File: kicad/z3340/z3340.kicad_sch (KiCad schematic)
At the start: 43 parts, among them J1 Conn_01x01, J2 Conn_01x02, J3 Conn_02x20_Odd_Even, Q3 MMBT3904, U1 DG442CY+, U10 AS3364, U11 PCA9555D, U13 TL074, U14 DG406, U15 M24C02-WMN, U5 TL074, U8 DG442CY+, U9 TL072

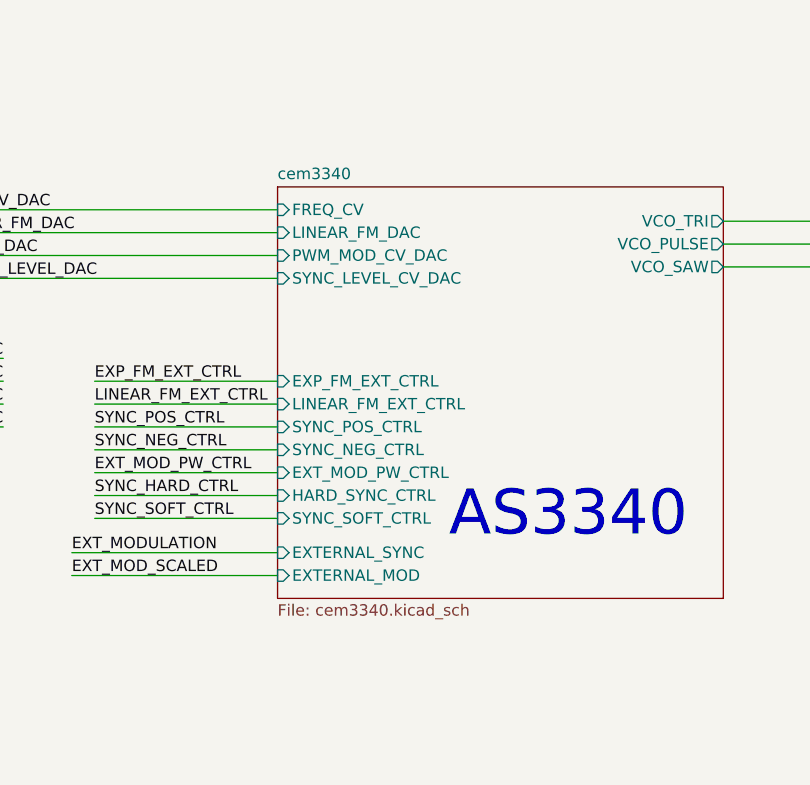
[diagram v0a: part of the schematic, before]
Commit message: continue file renaming
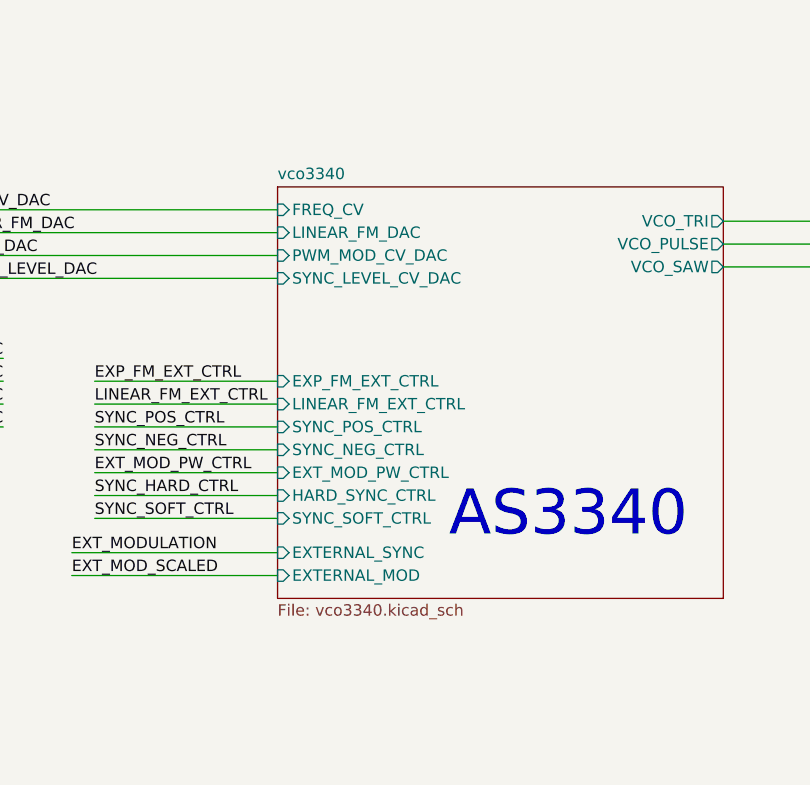
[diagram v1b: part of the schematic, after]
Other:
- sheet cem3340 renamed vco3340
- sheet vco3340: file cem3340.kicad_sch -> vco3340.kicad_sch

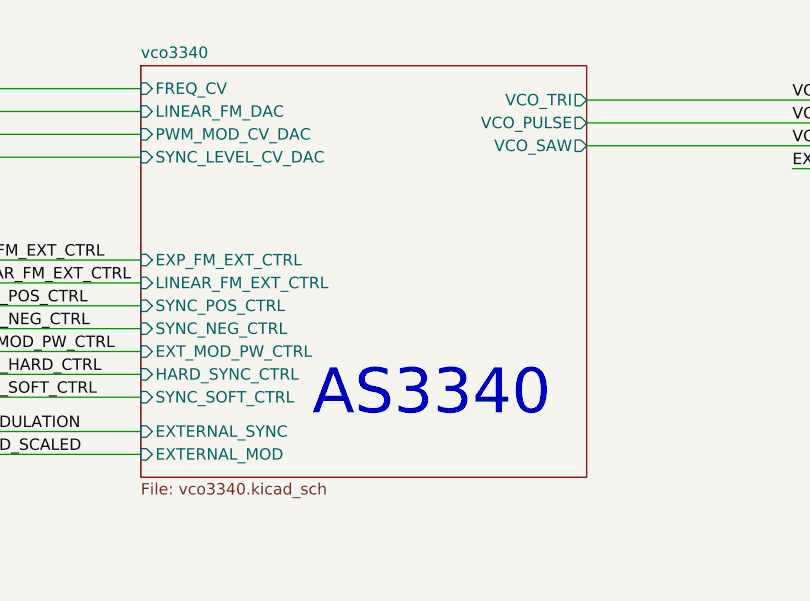
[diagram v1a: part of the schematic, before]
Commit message: cleanup references after file renaming
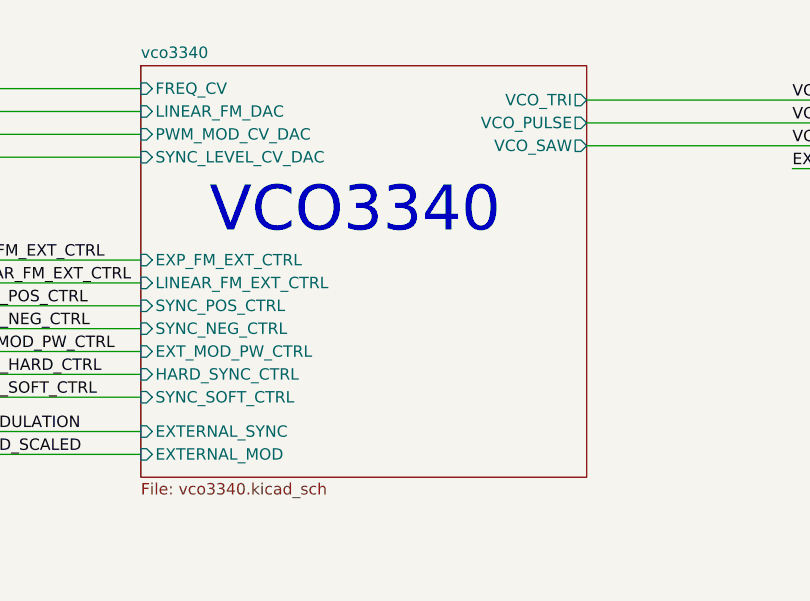
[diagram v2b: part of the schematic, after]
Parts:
- U10: symbol as3340:AS3364 -> z3340:AS3364
- U14: symbol as3340:DG406 -> z3340:DG406
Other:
- note added: "VCO3340"
- note removed: "AS3340"
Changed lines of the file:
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@@
     (effects (font (size 1.27 1.27)) (justify left bottom))
   )
-  (text "AS3340" (at 157.48 165.1 0)
+  (text "VCO3340" (at 146.05 144.78 0)
     (effects (font (size 5.0038 5.0038)) (justify left bottom))
   )
@@
     )
   )
-  (symbol (lib_id "as3340:DG406") (at 281.94 66.04 0) (unit 1)
+  (symbol (lib_id "z3340:DG406") (at 281.94 66.04 0) (unit 1)
     (in_bom yes) (on_board yes) (dnp no)
     (property "Reference" "U14" (at 279.4 64.77 0)
@@
     )
   )
-  (symbol (lib_id "as3340:AS3364") (at 125.73 236.22 0) (unit 1)
+  (symbol (lib_id "z3340:AS3364") (at 125.73 236.22 0) (unit 1)
     (in_bom yes) (on_board yes) (dnp no) (fields_autoplaced)
     (property "Reference" "U10" (at 132.7912 236.2779 0)

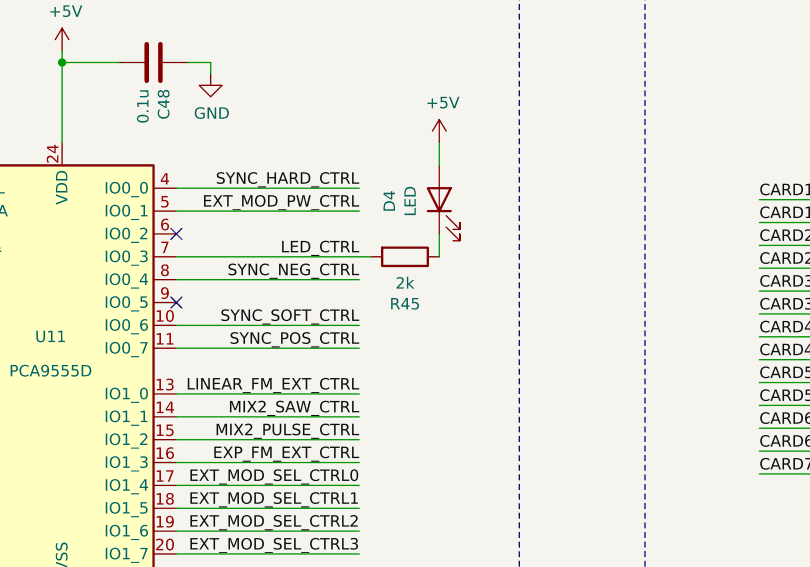
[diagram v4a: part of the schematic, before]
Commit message: updates for v0.9: polygons, LED resistor, mod amount
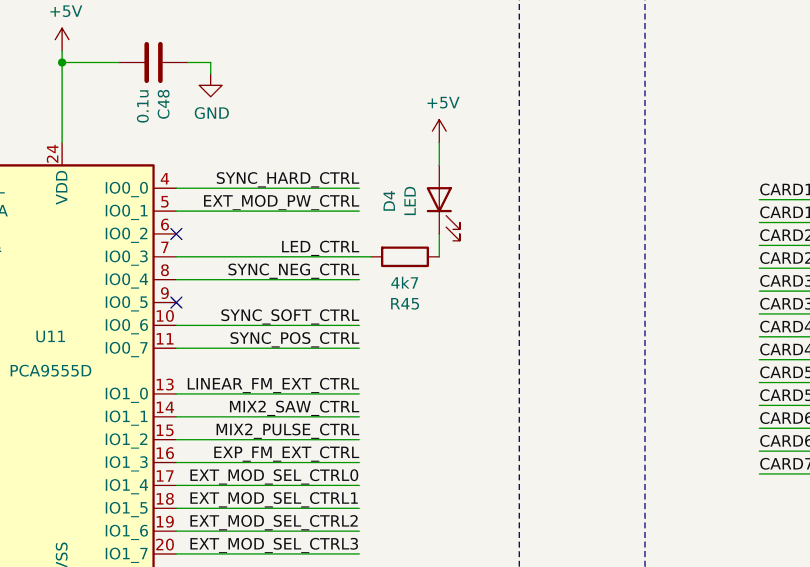
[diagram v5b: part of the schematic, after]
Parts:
- C12, C13, C19, C21, C22, C27, C37, C38, C40, C43, C44, C45, C46, C47, C48, C9: LCSC (none) -> C14663; LCSC Part C14663 -> (none)
- C30: LCSC (none) -> C53987; LCSC Part C53987 -> (none)
- D4: LCSC (none) -> C2286; LCSC Part C2286 -> (none)
- Q3: LCSC (none) -> C20526; LCSC Part C20526 -> (none)
- R40: LCSC (none) -> C22775; LCSC Part C22775 -> (none)
- R45: value 2k -> 4k7; LCSC (none) -> C23162; LCSC Part C22975 -> (none)
- R48, R65: LCSC (none) -> C25804; LCSC Part C25804 -> (none)
- R51, R57, R58: LCSC (none) -> C25803; LCSC Part C25803 -> (none)
- U1, U8: LCSC (none) -> C2673321; LCSC Part C2673321 -> (none)
- U11: LCSC (none) -> C83265; LCSC Part C83265 -> (none)
- U13, U5: LCSC (none) -> C96507; LCSC Part C96507 -> (none)
- U14: LCSC (none) -> C426318; LCSC Part C426318 -> (none)
- U15: LCSC (none) -> C7562; LCSC Part C7562 -> (none)
- U9: LCSC (none) -> C6961; LCSC Part C6961 -> (none)
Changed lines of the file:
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@@
   (title_block
     (title "Zoxnoxious 3340 Oscillator")
-    (date "2024-07-15")
-    (rev "0.8")
+    (date "2025-02-06")
+    (rev "0.9")
     (company "Zoxnoxious Engineering")
   )
@@
       (effects (font (size 1.27 1.27)) hide)
     )
-    (property "LCSC Part" "C14663" (at 189.23 29.21 0)
+    (property "LCSC" "C14663" (at 189.23 29.21 0)
       (effects (font (size 1.27 1.27)) hide)
     )
@@
       (effects (font (size 1.27 1.27)) hide)
     )
-    (property "LCSC Part" "C83265" (at 179.07 63.5 0)
+    (property "LCSC" "C83265" (at 179.07 63.5 0)
       (effects (font (size 1.27 1.27)) hide)
     )
@@
       (effects (font (size 1.27 1.27)))
     )
-    (property "Value" "2k" (at 217.17 53.7464 90)
+    (property "Value" "4k7" (at 217.17 53.7464 90)
       (effects (font (size 1.27 1.27)))
     )
@@
       (effects (font (size 1.27 1.27)) hide)
     )
-    (property "LCSC Part" "C22975" (at 217.17 50.8 0)
+    (property "LCSC" "C23162" (at 217.17 50.8 0)
       (effects (font (size 1.27 1.27)) hide)
     )
@@
       (effects (font (size 1.27 1.27)) hide)
     )
-    (property "LCSC Part" "C2286" (at 220.98 44.45 0)
+    (property "LCSC" "C2286" (at 220.98 44.45 0)
       (effects (font (size 1.27 1.27)) hide)
     )
@@
       (effects (font (size 1.27 1.27)) hide)
     )
-    (property "LCSC Part" "C14663" (at 386.08 29.21 0)
+    (property "LCSC" "C14663" (at 386.08 29.21 0)
       (effects (font (size 1.27 1.27)) hide)
     )
@@
       (effects (font (size 1.27 1.27)) hide)
     )
-    (property "LCSC Part" "C7562" (at 379.73 43.18 0)
+    (property "LCSC" "C7562" (at 379.73 43.18 0)
       (effects (font (size 1.27 1.27)) hide)
     )
@@
       (effects (font (size 1.27 1.27)) hide)
     )
-    (property "LCSC Part" "C14663" (at 153.67 231.14 0)
+    (property "LCSC" "C14663" (at 153.67 231.14 0)
       (effects (font (size 1.27 1.27)) hide)
     )
@@
       (effects (font (size 1.27 1.27)) hide)
     )
-    (property "LCSC Part" "C14663" (at 153.67 242.57 0)
+    (property "LCSC" "C14663" (at 153.67 242.57 0)
       (effects (font (size 1.27 1.27)) hide)
     )
@@
       (effects (font (size 1.27 1.27)) hide)
     )
-    (property "LCSC Part" "C2673321" (at 165.1 237.49 0)
+    (property "LCSC" "C2673321" (at 165.1 237.49 0)
       (effects (font (size 1.27 1.27)) hide)
     )
@@
       (effects (font (size 1.27 1.27)) hide)
     )
-    (property "LCSC Part" "C14663" (at 179.07 231.14 0)
+    (property "LCSC" "C14663" (at 179.07 231.14 0)
       (effects (font (size 1.27 1.27)) hide)
     )
@@
       (effects (font (size 1.27 1.27)) hide)
     )
-    (property "LCSC Part" "C14663" (at 179.07 242.57 0)
+    (property "LCSC" "C14663" (at 179.07 242.57 0)
       (effects (font (size 1.27 1.27)) hide)
     )
@@
       (effects (font (size 1.27 1.27)) hide)
     )
-    (property "LCSC Part" "C2673321" (at 190.5 237.49 0)
+    (property "LCSC" "C2673321" (at 190.5 237.49 0)
       (effects (font (size 1.27 1.27)) hide)
     )
@@
       (effects (font (size 1.27 1.27)) hide)
     )
-    (property "LCSC Part" "C14663" (at 125.73 254 0)
+    (property "LCSC" "C14663" (at 125.73 254 0)
       (effects (font (size 1.27 1.27)) hide)
     )
@@
       (effects (font (size 1.27 1.27)) hide)
     )
-    (property "LCSC Part" "C426318" (at 281.94 66.04 0)
+    (property "LCSC" "C426318" (at 281.94 66.04 0)
       (effects (font (size 1.27 1.27)) hide)
     )
@@
       (effects (font (size 1.27 1.27)) hide)
     )
-    (property "LCSC Part" "C25804" (at 332.74 207.01 0)
+    (property "LCSC" "C25804" (at 332.74 207.01 0)
       (effects (font (size 1.27 1.27)) hide)
     )
@@
       (effects (font (size 1.27 1.27)) hide)
     )
-    (property "LCSC Part" "C96507" (at 397.51 217.17 0)
+    (property "LCSC" "C96507" (at 397.51 217.17 0)
       (effects (font (size 1.27 1.27)) hide)
     )
@@
       (effects (font (size 1.27 1.27)) hide)
     )
-    (property "LCSC Part" "C14663" (at 270.51 29.21 0)
+    (property "LCSC" "C14663" (at 270.51 29.21 0)
       (effects (font (size 1.27 1.27)) hide)
     )
@@
       (effects (font (size 1.27 1.27)) hide)
     )
-    (property "LCSC Part" "C22775" (at 115.57 240.03 0)
+    (property "LCSC" "C22775" (at 115.57 240.03 0)
       (effects (font (size 1.27 1.27)) hide)
     )
@@
       (effects (font (size 1.27 1.27)) hide)
     )
-    (property "LCSC Part" "C6961" (at 317.5 53.34 0)
+    (property "LCSC" "C6961" (at 317.5 53.34 0)
       (effects (font (size 1.27 1.27)) hide)
     )
@@
       (effects (font (size 1.27 1.27)) hide)
     )
-    (property "LCSC Part" "C14663" (at 58.42 246.38 0)
+    (property "LCSC" "C14663" (at 58.42 246.38 0)
       (effects (font (size 1.27 1.27)) hide)
     )
@@
       (effects (font (size 1.27 1.27)) hide)
     )
-    (property "LCSC Part" "C6961" (at 99.06 238.76 0)
+    (property "LCSC" "C6961" (at 99.06 238.76 0)
       (effects (font (size 1.27 1.27)) hide)
     )
@@
       (effects (font (size 1.27 1.27)) (justify left) hide)
     )
-    (property "LCSC Part" "C20526" (at 330.2 218.44 0)
+    (property "LCSC" "C20526" (at 330.2 218.44 0)
       (effects (font (size 1.27 1.27)) hide)
     )
@@
       (effects (font (size 1.27 1.27)) hide)
     )
-    (property "LCSC Part" "C96507" (at 40.64 238.76 0)
+    (property "LCSC" "C96507" (at 40.64 238.76 0)
       (effects (font (size 1.27 1.27)) hide)
     )
@@
       (effects (font (size 1.27 1.27)) hide)
     )
-    (property "LCSC Part" "C14663" (at 86.36 234.95 0)
+    (property "LCSC" "C14663" (at 86.36 234.95 0)
       (effects (font (size 1.27 1.27)) hide)
     )
@@
       (effects (font (size 1.27 1.27)) hide)
     )
-    (property "LCSC Part" "C25803" (at 299.72 50.8 0)
+    (property "LCSC" "C25803" (at 299.72 50.8 0)
       (effects (font (size 1.27 1.27)) hide)
     )
@@
       (effects (font (size 1.27 1.27)) hide)
     )
-    (property "LCSC Part" "C14663" (at 86.36 246.38 0)
+    (property "LCSC" "C14663" (at 86.36 246.38 0)
       (effects (font (size 1.27 1.27)) hide)
     )
@@
       (effects (font (size 1.27 1.27)) hide)
     )
-    (property "LCSC Part" "C25803" (at 316.23 218.44 0)
+    (property "LCSC" "C25803" (at 316.23 218.44 0)
       (effects (font (size 1.27 1.27)) hide)
     )
@@
       (effects (font (size 1.27 1.27)) hide)
     )
-    (property "LCSC Part" "C25803" (at 314.96 43.18 0)
+    (property "LCSC" "C25803" (at 314.96 43.18 0)
       (effects (font (size 1.27 1.27)) hide)
     )
@@
       (effects (font (size 1.27 1.27)) hide)
     )
-    (property "LCSC" "" (at 27.94 246.38 0)
+    (property "LCSC" "C14663" (at 27.94 246.38 0)
       (effects (font (size 1.27 1.27)) hide)
     )
-    (property "LCSC Part" "C14663" (at 27.94 246.38 0)
+    (property "LCSC" "C14663" (at 27.94 246.38 0)
       (effects (font (size 1.27 1.27)) hide)
     )
@@
       (effects (font (size 1.27 1.27)) hide)
     )
-    (property "LCSC Part" "C14663" (at 133.35 226.06 0)
+    (property "LCSC" "C14663" (at 133.35 226.06 0)
       (effects (font (size 1.27 1.27)) hide)
     )
@@
       (effects (font (size 1.27 1.27)) hide)
     )
-    (property "LCSC Part" "C96507" (at 71.12 238.76 0)
+    (property "LCSC" "C96507" (at 71.12 238.76 0)
       (effects (font (size 1.27 1.27)) hide)
     )
@@
       (effects (font (size 1.27 1.27)) hide)
     )
-    (property "LCSC Part" "C14663" (at 58.42 234.95 0)
+    (property "LCSC" "C14663" (at 58.42 234.95 0)
       (effects (font (size 1.27 1.27)) hide)
     )
@@
       (effects (font (size 1.27 1.27)) hide)
     )
-    (property "LCSC Part" "C53987" (at 115.57 250.19 0)
+    (property "LCSC" "C53987" (at 115.57 250.19 0)
       (effects (font (size 1.27 1.27)) hide)
     )
@@
       (effects (font (size 1.27 1.27)) hide)
     )
-    (property "LCSC Part" "C14663" (at 292.1 29.21 0)
+    (property "LCSC" "C14663" (at 292.1 29.21 0)
       (effects (font (size 1.27 1.27)) hide)
     )
@@
       (effects (font (size 1.27 1.27)) hide)
     )
-    (property "LCSC" "" (at 27.94 234.95 0)
+    (property "LCSC" "C14663" (at 27.94 234.95 0)
       (effects (font (size 1.27 1.27)) hide)
     )
-    (property "LCSC Part" "C14663" (at 27.94 234.95 0)
+    (property "LCSC" "C14663" (at 27.94 234.95 0)
       (effects (font (size 1.27 1.27)) hide)
     )
@@
       (effects (font (size 1.27 1.27)) hide)
     )
-    (property "LCSC Part" "C25804" (at 398.78 41.91 0)
+    (property "LCSC" "C25804" (at 398.78 41.91 0)
       (effects (font (size 1.27 1.27)) hide)
     )
